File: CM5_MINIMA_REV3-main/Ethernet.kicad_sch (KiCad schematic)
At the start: 7 parts, among them J1 GLPLX-SMT-188S7, U401 TPD4EUSB30, U402 TPD4EUSB30

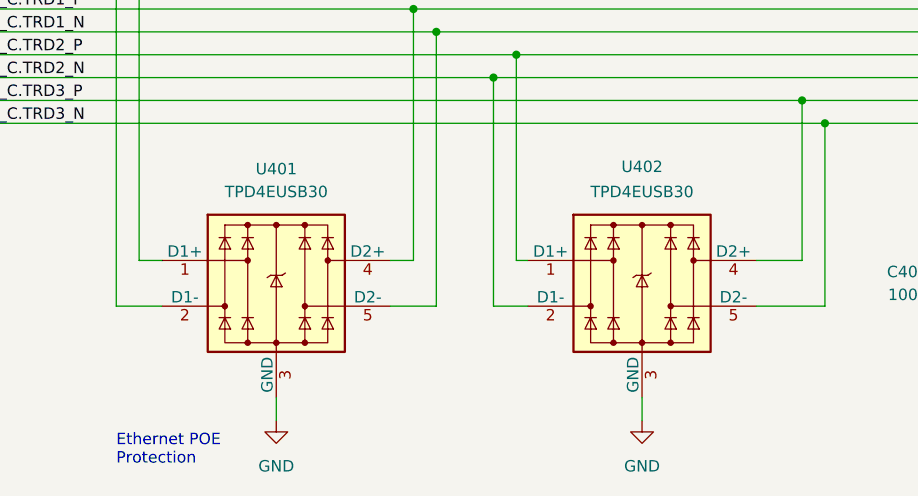
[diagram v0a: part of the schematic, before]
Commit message: warning fix - 17 left
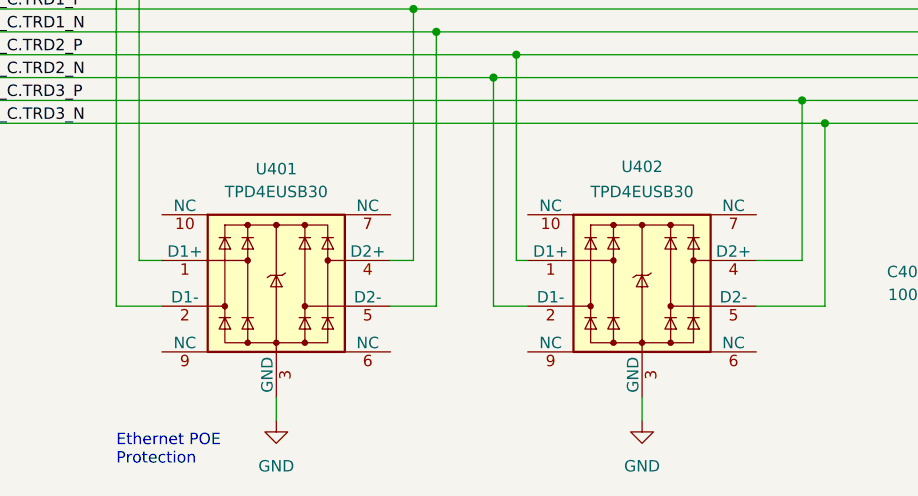
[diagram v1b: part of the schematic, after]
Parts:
- J1: footprint Samacsys:GLPLXSMT188S7QQYG -> CM5_MINIMA_local:GLPLXSMT188S7QQYG
- U401, U402: symbol CM4IO:TPD4EUSB30 -> Power_Protection:TPD4EUSB30
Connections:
- net ETH_C.TRD0_N: no longer U401.9
- net ETH_C.TRD0_P: no longer U401.10
- net ETH_C.TRD1_N: no longer U401.6
- net ETH_C.TRD1_P: no longer U401.7
- net ETH_C.TRD2_N: no longer U402.9
- net ETH_C.TRD2_P: no longer U402.10
- net ETH_C.TRD3_N: no longer U402.6
- net ETH_C.TRD3_P: no longer U402.7
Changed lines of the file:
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@@
 			)
 		)
-		(property "Footprint" "Samacsys:GLPLXSMT188S7QQYG"
+		(property "Footprint" "CM5_MINIMA_local:GLPLXSMT188S7QQYG"
 			(at 175.26 138.1 0)
 			(effects
@@
 	)
 	(symbol
-		(lib_id "CM4IO:TPD4EUSB30")
+		(lib_id "Power_Protection:TPD4EUSB30")
 		(at 100.33 81.28 0)
 		(unit 1)
@@
 			)
 		)
-		(property "Datasheet" ""
+		(property "Datasheet" "http://www.ti.com/lit/ds/symlink/tpd2eusb30a.pdf"
 			(at 100.33 81.28 0)
 			(effects
@@
 			)
 		)
-		(property "Description" ""
+		(property "Description" "4-Channel ESD Protection for Super-Speed USB 3.0 Interface, USON-10"
 			(at 100.33 81.28 0)
 			(effects
@@
 	)
 	(symbol
-		(lib_id "CM4IO:TPD4EUSB30")
+		(lib_id "Power_Protection:TPD4EUSB30")
 		(at 59.69 81.28 0)
 		(unit 1)
@@
 			)
 		)
-		(property "Datasheet" ""
+		(property "Datasheet" "http://www.ti.com/lit/ds/symlink/tpd2eusb30a.pdf"
 			(at 59.69 81.28 0)
 			(effects
@@
 			)
 		)
-		(property "Description" ""
+		(property "Description" "4-Channel ESD Protection for Super-Speed USB 3.0 Interface, USON-10"
 			(at 59.69 81.28 0)
 			(effects

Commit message: warning fix - 0  in schematic
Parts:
- J1: MPN (none) -> GLPLX-SMT-188S7-QQ-Y/G; Manufacturer (none) -> Kycon
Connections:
- net ETH_C.TRD0_N: now also J1.J2 (TX1-)
- net ETH_C.TRD0_P: now also J1.J1 (TX1+)
- net ETH_C.TRD1_N: now also J1.J6 (TX2-)
- net ETH_C.TRD1_P: now also J1.J3 (TX2+)
- net ETH_C.TRD2_N: now also J1.J5 (TX3-)
- net ETH_C.TRD2_P: now also J1.J4 (TX3+)
- net ETH_C.TRD3_N: now also J1.J8 (TX4-)
- net ETH_C.TRD3_P: now also J1.J7 (TX4+)
- net at R401.2: now also J1.14 (LED_G-); no longer J1.11 (K_GREEN)
- removed net +3V3_PI: J1.12 (A_GREEN), J1.14 (A_YELLOW)
- new net: J1.SH (SHIELD), R403.1
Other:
- moved on the sheet: R401, R402, R403

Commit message: Revert CM5_MINIMA_REV3-main to pre-warning-fix state (feae2c2) - fix component mismatches
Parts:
- J1: footprint CM5_MINIMA_local:GLPLXSMT188S7QQYG -> Samacsys:GLPLXSMT188S7QQYG; MPN GLPLX-SMT-188S7-QQ-Y/G -> (none); Manufacturer Kycon -> (none)
- U401, U402: symbol Power_Protection:TPD4EUSB30 -> CM4IO:TPD4EUSB30
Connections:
- net ETH_C.TRD0_N: now also U401.9; no longer J1.J2 (TX1-)
- net ETH_C.TRD0_P: now also U401.10; no longer J1.J1 (TX1+)
- net ETH_C.TRD1_N: now also U401.6; no longer J1.J6 (TX2-)
- net ETH_C.TRD1_P: now also U401.7; no longer J1.J3 (TX2+)
- net ETH_C.TRD2_N: now also U402.9; no longer J1.J5 (TX3-)
- net ETH_C.TRD2_P: now also U402.10; no longer J1.J4 (TX3+)
- net ETH_C.TRD3_N: now also U402.6; no longer J1.J8 (TX4-)
- net ETH_C.TRD3_P: now also U402.7; no longer J1.J7 (TX4+)
- net at R401.2: now also J1.11 (K_GREEN); no longer J1.14 (LED_G-)
- net at R403.1: now also J1.15 (MP1), J1.16 (MP2); no longer J1.SH (SHIELD)
- new net +3V3_PI: J1.12 (A_GREEN), J1.14 (A_YELLOW)
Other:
- moved on the sheet: R401, R402, R403
